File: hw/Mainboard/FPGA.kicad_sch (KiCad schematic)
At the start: 60 parts, among them J5 PMOD1, J6 PMOD2, J7 PROG, J8 FPGA_MCU, J9 BUS_EXPANSION, Q1 MMBT3904, SW3 CONFIG, U10 T8Q144C3

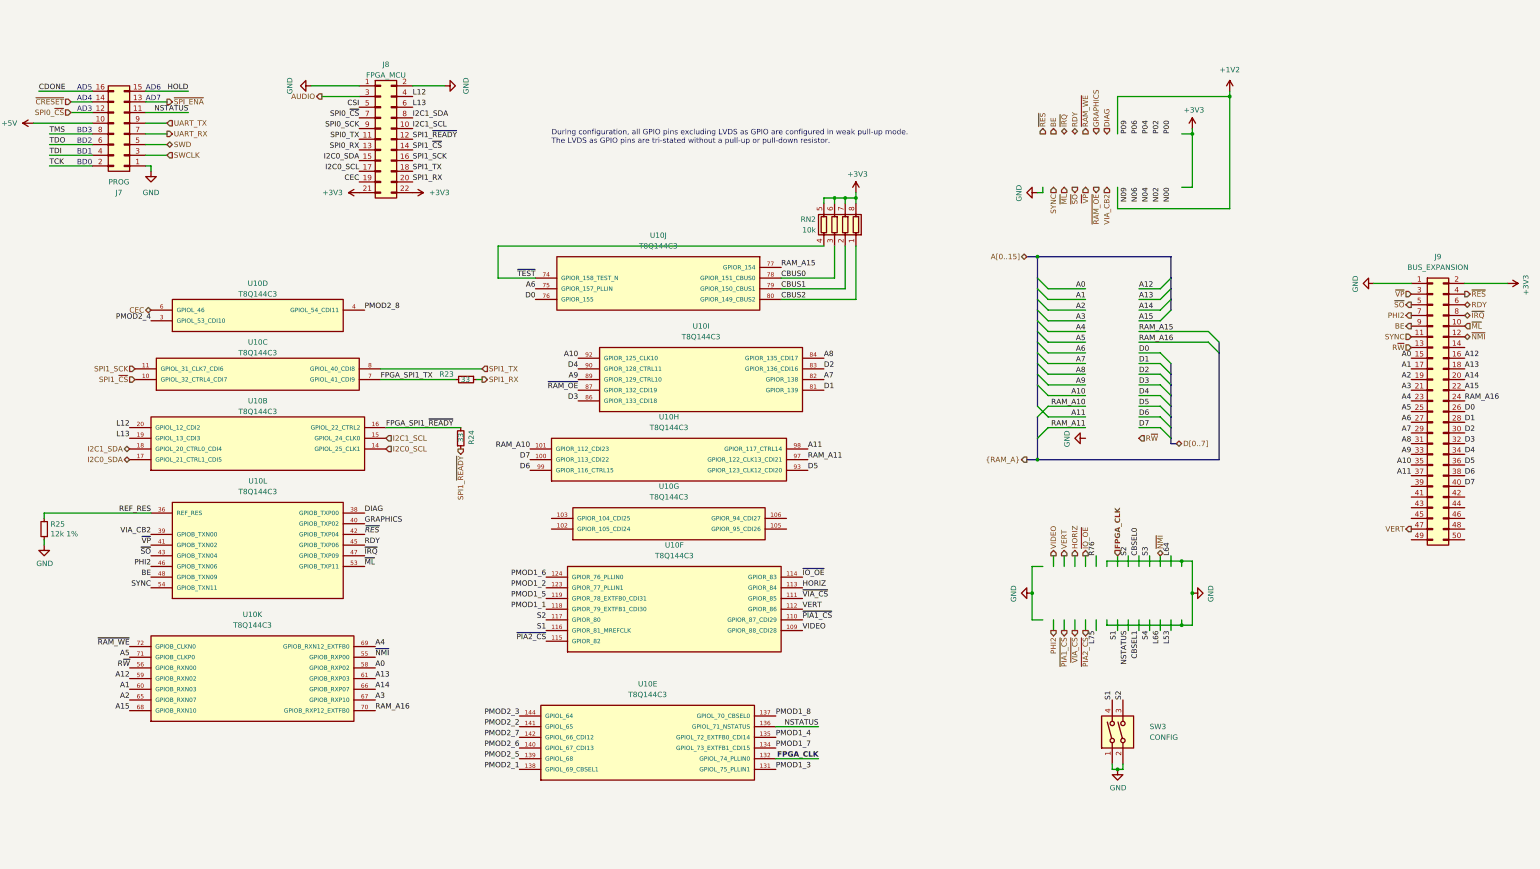
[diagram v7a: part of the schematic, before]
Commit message: hw: remove vp/ml pins
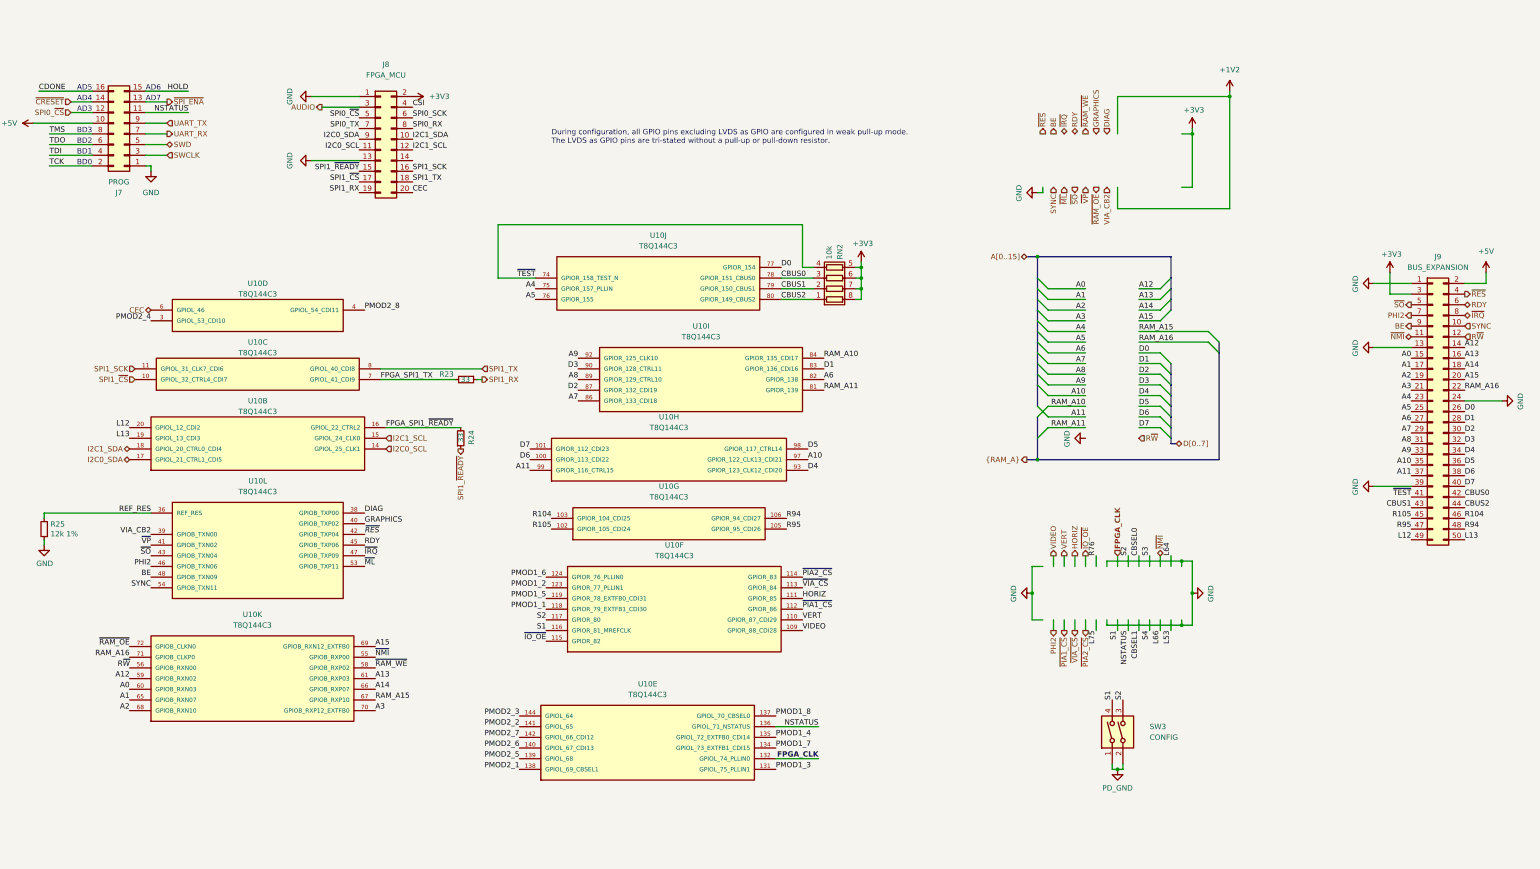
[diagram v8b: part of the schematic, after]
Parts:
- J8: footprint Connector_PinHeader_2.54mm:PinHeader_2x11_P2.54mm_Vertical -> Connector_PinHeader_2.54mm:PinHeader_2x10_P2.54mm_Vertical; symbol Connector_Generic:Conn_02x11_Odd_Even -> Connector_Generic:Conn_02x10_Odd_Even
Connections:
- net +3V3: now also J8.2 (Pin_2), J9.3 (Pin_3); no longer J8.21 (Pin_21), J8.22 (Pin_22), J9.2 (Pin_2)
- net +5V: now also J9.2 (Pin_2)
- net A0: now also U10.60 (GPIOB_RXN03); no longer U10.58 (GPIOB_RXP02)
- net A1: now also U10.65 (GPIOB_RXN07); no longer U10.60 (GPIOB_RXN03)
- net A10: now also U10.97 (GPIOR_122_CLK13_CDI21); no longer U10.92 (GPIOR_125_CLK10)
- net A11: now also U10.99 (GPIOR_116_CTRL15); no longer U10.98 (GPIOR_117_CTRL14)
- net A12: now also J9.14 (Pin_14); no longer J9.16 (Pin_16)
- net A13: now also J9.16 (Pin_16); no longer J9.18 (Pin_18)
- net A14: now also J9.18 (Pin_18); no longer J9.20 (Pin_20)
- net A15: now also J9.20 (Pin_20), U10.69 (GPIOB_RXN12_EXTFB0); no longer J9.22 (Pin_22), U10.68 (GPIOB_RXN10)
- net A2: now also U10.68 (GPIOB_RXN10); no longer U10.65 (GPIOB_RXN07)
- net A3: now also U10.70 (GPIOB_RXP12_EXTFB0); no longer U10.67 (GPIOB_RXP10)
- net A4: now also U10.75 (GPIOR_157_PLLIN); no longer U10.69 (GPIOB_RXN12_EXTFB0)
- net A5: now also U10.76 (GPIOR_155); no longer U10.71 (GPIOB_CLKP0)
- net A6: now also U10.82 (GPIOR_138); no longer U10.75 (GPIOR_157_PLLIN)
- net A7: now also U10.86 (GPIOR_133_CDI18); no longer U10.82 (GPIOR_138)
- net A8: now also U10.89 (GPIOR_129_CTRL10); no longer U10.84 (GPIOR_135_CDI17)
- net A9: now also U10.92 (GPIOR_125_CLK10); no longer U10.89 (GPIOR_129_CTRL10)
- net CBUS0: now also J9.42 (Pin_42)
- net CBUS1: now also J9.43 (Pin_43)
- net CBUS2: now also J9.44 (Pin_44)
- net CEC: now also J8.20 (Pin_20); no longer J8.19 (Pin_19)
- net CSI: now also J8.4 (Pin_4); no longer J8.5 (Pin_5)
- net D0: now also U10.77 (GPIOR_154); no longer U10.76 (GPIOR_155)
- net D1: now also U10.83 (GPIOR_136_CDI16); no longer U10.81 (GPIOR_139)
- net D2: now also U10.87 (GPIOR_132_CDI19); no longer U10.83 (GPIOR_136_CDI16)
- net D3: now also U10.90 (GPIOR_128_CTRL11); no longer U10.86 (GPIOR_133_CDI18)
- net D4: now also U10.93 (GPIOR_123_CLK12_CDI20); no longer U10.90 (GPIOR_128_CTRL11)
- net D5: now also U10.98 (GPIOR_117_CTRL14); no longer U10.93 (GPIOR_123_CLK12_CDI20)
- net D6: now also U10.100 (GPIOR_113_CDI22); no longer U10.99 (GPIOR_116_CTRL15)
- net D7: now also U10.101 (GPIOR_112_CDI23); no longer U10.100 (GPIOR_113_CDI22)
- net GND: now also J8.13 (Pin_13), J9.13 (Pin_13), J9.24 (Pin_24), J9.39 (Pin_39); no longer J8.2 (Pin_2), SW3.1, SW3.2
- net HORIZ: now also U10.111 (GPIOR_85); no longer U10.113 (GPIOR_84)
- net I2C0_SCL: now also J8.11 (Pin_11); no longer J8.17 (Pin_17)
- net I2C0_SDA: now also J8.9 (Pin_9); no longer J8.15 (Pin_15)
- net I2C1_SCL: now also J8.12 (Pin_12); no longer J8.10 (Pin_10)
- net I2C1_SDA: now also J8.10 (Pin_10); no longer J8.8 (Pin_8)
- net L12: now also J9.49 (Pin_49); no longer J8.4 (Pin_4)
- net L13: now also J9.50 (Pin_50); no longer J8.6 (Pin_6)
- net PD_GND: now also SW3.1, SW3.2
- net RAM_A10: now also U10.84 (GPIOR_135_CDI17); no longer U10.101 (GPIOR_112_CDI23)
- net RAM_A11: now also U10.81 (GPIOR_139); no longer U10.97 (GPIOR_122_CLK13_CDI21)
- net RAM_A15: now also U10.67 (GPIOB_RXP10); no longer U10.77 (GPIOR_154)
- net RAM_A16: now also J9.22 (Pin_22), U10.71 (GPIOB_CLKP0); no longer J9.24 (Pin_24), U10.70 (GPIOB_RXP12_EXTFB0)
- net R~{W}: now also J9.12 (Pin_12); no longer J9.13 (Pin_13)
- net SPI0_RX: now also J8.8 (Pin_8); no longer J8.13 (Pin_13)
- net SPI0_SCK: now also J8.6 (Pin_6); no longer J8.9 (Pin_9)
- net SPI0_TX: now also J8.7 (Pin_7); no longer J8.11 (Pin_11)
- net SPI0_~{CS}: now also J8.5 (Pin_5); no longer J8.7 (Pin_7)
- net SPI1_RX: now also J8.19 (Pin_19); no longer J8.20 (Pin_20)
- net SPI1_~{CS}: now also J8.17 (Pin_17); no longer J8.14 (Pin_14)
- net SPI1_~{READY}: now also J8.15 (Pin_15); no longer J8.12 (Pin_12)
- net SYNC: now also J9.10 (Pin_10); no longer J9.11 (Pin_11)
- net VERT: now also U10.110 (GPIOR_87_CDI29); no longer J9.47 (Pin_47), U10.112 (GPIOR_86)
- net ~{IO_OE}: now also U10.115 (GPIOR_82); no longer U10.114 (GPIOR_83)
- net ~{ML}: no longer J9.10 (Pin_10)
- net ~{NMI}: now also J9.11 (Pin_11); no longer J9.12 (Pin_12)
- net ~{PIA1_CS}: now also U10.112 (GPIOR_86); no longer U10.110 (GPIOR_87_CDI29)
- net ~{PIA2_CS}: now also U10.114 (GPIOR_83); no longer U10.115 (GPIOR_82)
- net ~{RAM_OE}: now also U10.72 (GPIOB_CLKN0); no longer U10.87 (GPIOR_132_CDI19)
- net ~{RAM_WE}: now also U10.58 (GPIOB_RXP02); no longer U10.72 (GPIOB_CLKN0)
- net ~{TEST}: now also J9.41 (Pin_41)
- net ~{VIA_CS}: now also U10.113 (GPIOR_84); no longer U10.111 (GPIOR_85)
- net ~{VP}: no longer J9.3 (Pin_3)
- net R105: now reaches J9.45 (Pin_45)
- net R105: now also U10.102 (GPIOR_105_CDI24)
- net R104: now reaches J9.46 (Pin_46)
- net R104: now also U10.103 (GPIOR_104_CDI25)
- net R94: now reaches J9.48 (Pin_48)
- net R94: now also U10.106 (GPIOR_94_CDI27)
- net R95: now reaches U10.105 (GPIOR_95_CDI26)
- net R95: now also J9.47 (Pin_47)
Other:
- moved on the sheet: RN2
